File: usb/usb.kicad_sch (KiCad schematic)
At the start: 14 parts, among them J101 DX07S016JA3, J102 2x05_Horizontal

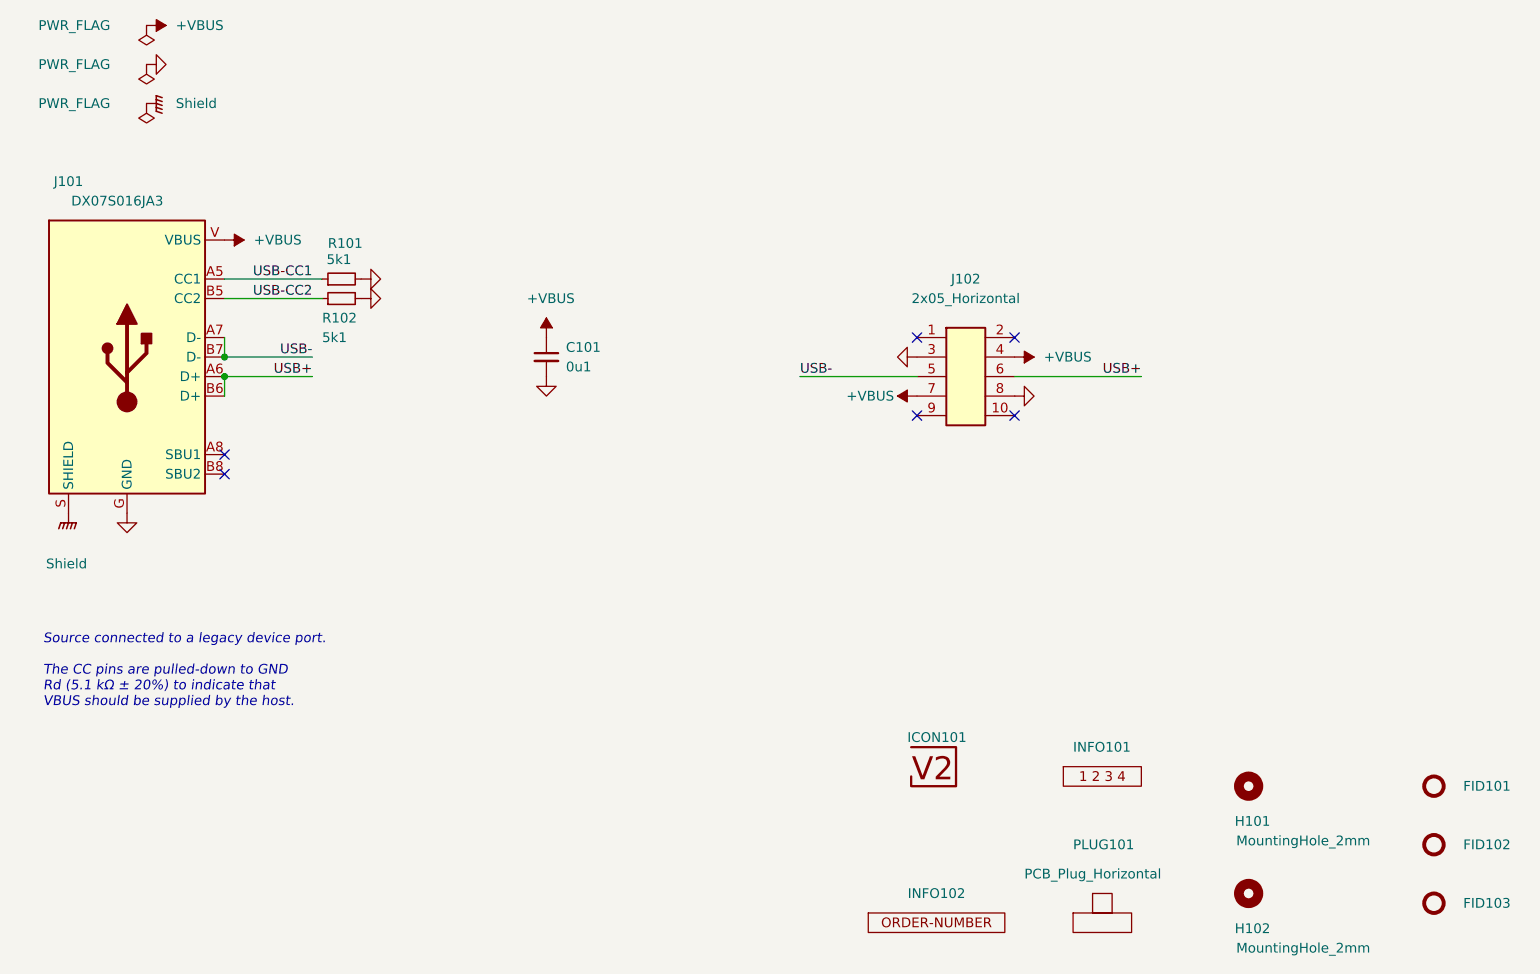
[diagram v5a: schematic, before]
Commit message: Replace Order_Number
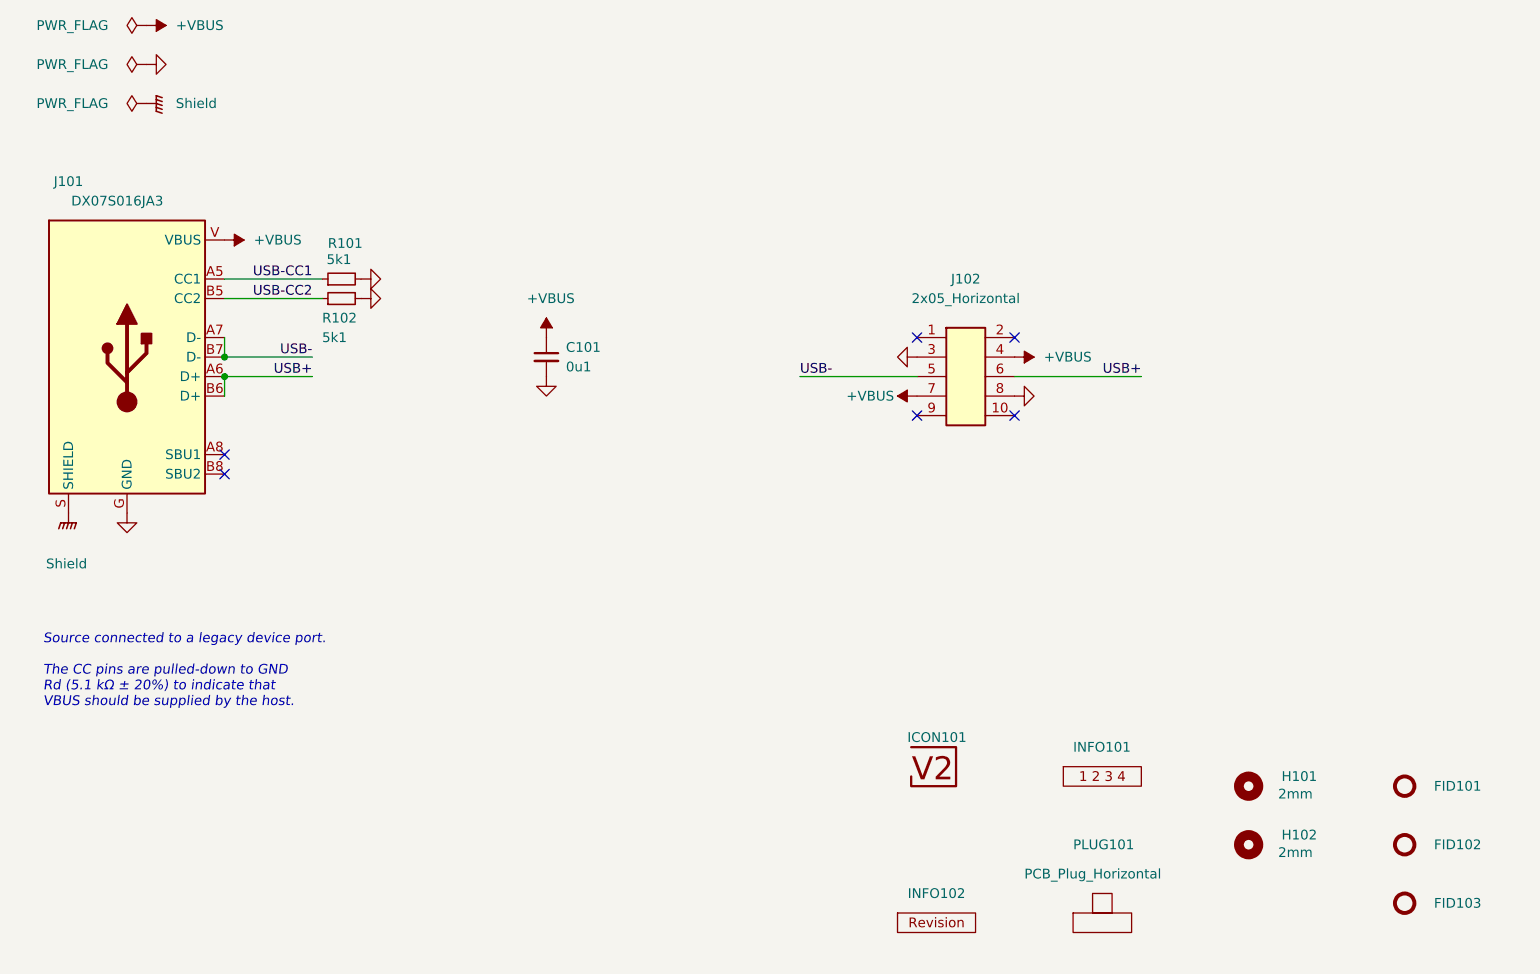
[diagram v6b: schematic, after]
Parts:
- H101, H102: value MountingHole_2mm -> 2mm
- INFO102: value Order_Number -> ~; footprint V2_Production:Order_Number -> V2_Production:Revision; symbol V2_Production:Order_Number -> V2_Production:Revision
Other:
- moved on the sheet: FID101, FID102, FID103, H102
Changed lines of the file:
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@@
 		(dnp no)
 		(property "Reference" "H101"
-			(at 246.888 162.052 0)
-			(effects
-				(font
-					(size 1.27 1.27)
-				)
-			)
-		)
-		(property "Value" "MountingHole_2mm"
-			(at 253.492 164.592 0)
+			(at 252.984 156.21 0)
+			(effects
+				(font
+					(size 1.27 1.27)
+				)
+			)
+		)
+		(property "Value" "2mm"
+			(at 252.476 158.496 0)
 			(effects
 				(font
@@
 			)
 		)
-		(property "Sim.Enable" "0"
-			(at 246.38 157.48 0)
-			(effects
-				(font
-					(size 1.27 1.27)
-				)
-				(hide yes)
-			)
-		)
 		(instances
 			(project "usb"
@@
 	(symbol
 		(lib_id "V2_power:PWR_FLAG")
-		(at 102.87 68.58 90)
+		(at 102.87 68.58 0)
 		(unit 1)
 		(exclude_from_sim no)
@@
 		(dnp no)
 		(property "Reference" "#FLG0103"
-			(at 100.965 68.58 0)
+			(at 102.87 66.675 0)
 			(effects
 				(font
@@
 		)
 		(property "Value" "PWR_FLAG"
-			(at 93.472 68.58 90)
+			(at 93.218 68.58 0)
 			(effects
 				(font
@@
 		)
 		(property "Description" "Special symbol for telling ERC where power comes from"
-			(at 120.142 68.58 0)
+			(at 102.87 85.852 0)
 			(effects
 				(font
@@
 	(symbol
 		(lib_id "V2_Mechanical:MountingHole_2mm")
-		(at 246.38 171.45 0)
+		(at 246.38 165.1 0)
 		(unit 1)
 		(exclude_from_sim no)
@@
 		(dnp no)
 		(property "Reference" "H102"
-			(at 246.888 176.022 0)
-			(effects
-				(font
-					(size 1.27 1.27)
-				)
-			)
-		)
-		(property "Value" "MountingHole_2mm"
-			(at 253.492 178.562 0)
+			(at 252.984 163.83 0)
+			(effects
+				(font
+					(size 1.27 1.27)
+				)
+			)
+		)
+		(property "Value" "2mm"
+			(at 252.476 166.116 0)
 			(effects
 				(font
@@
 		)
 		(property "Footprint" "V2_Mechanical:MountingHole_2mm"
-			(at 246.38 176.53 0)
-			(effects
-				(font
-					(size 1.27 1.27)
-				)
-				(hide yes)
-			)
-		)
-		(property "Datasheet" ""
-			(at 246.38 171.45 0)
+			(at 246.38 170.18 0)
+			(effects
+				(font
+					(size 1.27 1.27)
+				)
+				(hide yes)
+			)
+		)
+		(property "Datasheet" ""
+			(at 246.38 165.1 0)
 			(effects
 				(font
@@
 		)
 		(property "Description" "Mounting Hole without connection"
-			(at 246.38 171.45 0)
-			(effects
-				(font
-					(size 1.27 1.27)
-				)
-				(hide yes)
-			)
-		)
-		(property "Sim.Enable" "0"
-			(at 246.38 171.45 0)
+			(at 246.38 165.1 0)
 			(effects
 				(font
@@
 	(symbol
 		(lib_id "V2_power:PWR_FLAG")
-		(at 102.87 63.5 90)
+		(at 102.87 63.5 0)
 		(unit 1)
 		(exclude_from_sim no)
@@
 		(dnp no)
 		(property "Reference" "#FLG0102"
-			(at 100.965 63.5 0)
+			(at 102.87 61.595 0)
 			(effects
 				(font
@@
 		)
 		(property "Value" "PWR_FLAG"
-			(at 93.472 63.5 90)
+			(at 93.218 63.5 0)
 			(effects
 				(font
@@
 		)
 		(property "Description" "Special symbol for telling ERC where power comes from"
-			(at 120.142 63.5 0)
+			(at 102.87 80.772 0)
 			(effects
 				(font
@@
 		(at 227.33 173.99 0)
 		(unit 1)
-		(exclude_from_sim no)
+		(exclude_from_sim yes)
 		(in_bom no)
 		(on_board yes)
@@
 			)
 		)
-		(property "Sim.Enable" "0"
-			(at 227.33 173.99 0)
-			(effects
-				(font
-					(size 1.27 1.27)
-				)
-				(hide yes)
-			)
-		)
 		(instances
 			(project "usb"
@@
 	)
 	(symbol
-		(lib_id "V2_Production:Order_Number")
+		(lib_id "V2_Production:Revision")
 		(at 205.74 175.26 0)
 		(unit 1)
@@
 			)
 		)
-		(property "Value" "Order_Number"
+		(property "Value" "~"
 			(at 205.74 177.8 0)
 			(effects
@@
 			)
 		)
-		(property "Footprint" "V2_Production:Order_Number"
+		(property "Footprint" "V2_Production:Revision"
 			(at 205.74 180.34 0)
 			(effects
@@
 	(symbol
 		(lib_id "V2_Mechanical:Fiducial_Paste")
-		(at 270.51 157.48 0)
+		(at 266.7 157.48 0)
 		(unit 1)
 		(exclude_from_sim no)
@@
 		(dnp no)
 		(property "Reference" "FID101"
-			(at 274.32 157.48 0)
+			(at 270.51 157.48 0)
 			(effects
 				(font
@@
 		)
 		(property "Value" "Fiducial_Paste"
-			(at 267.97 153.67 0)
+			(at 264.16 153.67 0)
 			(effects
 				(font
@@
 		)
 		(property "Footprint" "V2_Fiducial:Fiducial_0.5mm_Mask1mm_Paste"
-			(at 270.51 162.56 0)
-			(effects
-				(font
-					(size 1.27 1.27)
-				)
-				(hide yes)
-			)
-		)
-		(property "Datasheet" ""
-			(at 270.51 157.48 0)
+			(at 266.7 162.56 0)
+			(effects
+				(font
+					(size 1.27 1.27)
+				)
+				(hide yes)
+			)
+		)
+		(property "Datasheet" ""
+			(at 266.7 157.48 0)
 			(effects
 				(font
@@
 		)
 		(property "Description" "Fiducial Marker"
-			(at 270.51 157.48 0)
+			(at 266.7 157.48 0)
 			(effects
 				(font
@@
 	(symbol
 		(lib_id "V2_Mechanical:Fiducial_Paste")
-		(at 270.51 165.1 0)
+		(at 266.7 165.1 0)
 		(unit 1)
 		(exclude_from_sim no)
@@
 		(dnp no)
 		(property "Reference" "FID102"
-			(at 274.32 165.1 0)
+			(at 270.51 165.1 0)
 			(effects
 				(font
@@
 		)
 		(property "Value" "Fiducial_Paste"
-			(at 271.78 161.29 0)
+			(at 267.97 161.29 0)
 			(effects
 				(font
@@
 		)
 		(property "Footprint" "V2_Fiducial:Fiducial_0.5mm_Mask1mm_Paste"
-			(at 270.51 170.18 0)
-			(effects
-				(font
-					(size 1.27 1.27)
-				)
-				(hide yes)
-			)
-		)
-		(property "Datasheet" ""
-			(at 270.51 165.1 0)
+			(at 266.7 170.18 0)
+			(effects
+				(font
+					(size 1.27 1.27)
+				)
+				(hide yes)
+			)
+		)
+		(property "Datasheet" ""
+			(at 266.7 165.1 0)
 			(effects
 				(font
@@
 		)
 		(property "Description" "Fiducial Marker"
-			(at 270.51 165.1 0)
+			(at 266.7 165.1 0)
 			(effects
 				(font
@@
 	(symbol
 		(lib_id "V2_power:PWR_FLAG")
-		(at 102.87 58.42 90)
+		(at 102.87 58.42 0)
 		(unit 1)
 		(exclude_from_sim no)
@@
 		(dnp no)
 		(property "Reference" "#FLG0101"
-			(at 100.965 58.42 0)
+			(at 102.87 56.515 0)
 			(effects
 				(font
@@
 		)
 		(property "Value" "PWR_FLAG"
-			(at 93.472 58.42 90)
+			(at 93.218 58.42 0)
 			(effects
 				(font
@@
 		)
 		(property "Description" "Special symbol for telling ERC where power comes from"
-			(at 120.142 58.42 0)
+			(at 102.87 75.692 0)
 			(effects
 				(font
@@
 	(symbol
 		(lib_id "V2_Mechanical:Fiducial_Paste")
-		(at 270.51 172.72 0)
+		(at 266.7 172.72 0)
 		(unit 1)
 		(exclude_from_sim no)
@@
 		(dnp no)
 		(property "Reference" "FID103"
-			(at 274.32 172.72 0)
+			(at 270.51 172.72 0)
 			(effects
 				(font
@@
 		)
 		(property "Value" "Fiducial_Paste"
-			(at 267.97 168.91 0)
+			(at 264.16 168.91 0)
 			(effects
 				(font
@@
 		)
 		(property "Footprint" "V2_Fiducial:Fiducial_0.5mm_Mask1mm_Paste"
-			(at 270.51 177.8 0)
-			(effects
-				(font
-					(size 1.27 1.27)
-				)
-				(hide yes)
-			)
-		)
-		(property "Datasheet" ""
-			(at 270.51 172.72 0)
+			(at 266.7 177.8 0)
+			(effects
+				(font
+					(size 1.27 1.27)
+				)
+				(hide yes)
+			)
+		)
+		(property "Datasheet" ""
+			(at 266.7 172.72 0)
 			(effects
 				(font
@@
 		)
 		(property "Description" "Fiducial Marker"
-			(at 270.51 172.72 0)
+			(at 266.7 172.72 0)
 			(effects
 				(font
@@
 			(at 205.74 154.94 0)
 			(effects
-				(font
-					(size 1.27 1.27)
-				)
-				(hide yes)
-			)
-		)
-		(property "Sim.Enable" "0"
-			(at 205.74 154.94 0)
-			(effects

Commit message: Update Library
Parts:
- C101: symbol V2_Device:C_0603_0u1 -> V2_Capacitor:0603_0u1
- R101, R102: symbol V2_Device:R_0603_5k1 -> V2_Resistor:0603_5k1
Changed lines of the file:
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@@
 	)
 	(symbol
-		(lib_id "V2_Device:R_0603_5k1")
+		(lib_id "V2_Resistor:0603_5k1")
 		(at 128.27 91.44 90)
 		(unit 1)
@@
 		(dnp no)
 		(fields_autoplaced yes)
-		(property "Reference" "#PWR0106"
+		(property "Reference" "#PWR106"
 			(at 137.16 93.98 0)
 			(effects
@@
 			(project "usb"
 				(path "/6c8448b4-b04d-47e1-934e-e40cbe27a7be"
-					(reference "#PWR0106")
+					(reference "#PWR106")
 					(unit 1)
 				)
@@
 		(dnp no)
 		(fields_autoplaced yes)
-		(property "Reference" "#PWR0105"
+		(property "Reference" "#PWR105"
 			(at 137.16 91.44 0)
 			(effects
@@
 			(project "usb"
 				(path "/6c8448b4-b04d-47e1-934e-e40cbe27a7be"
-					(reference "#PWR0105")
+					(reference "#PWR105")
 					(unit 1)
 				)
@@
 		(on_board yes)
 		(dnp no)
-		(property "Reference" "#PWR0111"
+		(property "Reference" "#PWR111"
 			(at 207.01 106.68 0)
 			(effects
@@
 			(project "usb"
 				(path "/6c8448b4-b04d-47e1-934e-e40cbe27a7be"
-					(reference "#PWR0111")
+					(reference "#PWR111")
 					(unit 1)
 				)
@@
 		(on_board yes)
 		(dnp no)
-		(property "Reference" "#FLG0103"
+		(property "Reference" "#FLG103"
 			(at 102.87 66.675 0)
 			(effects
@@
 			(project "usb"
 				(path "/6c8448b4-b04d-47e1-934e-e40cbe27a7be"
-					(reference "#FLG0103")
+					(reference "#FLG103")
 					(unit 1)
 				)
@@
 		(on_board yes)
 		(dnp no)
-		(property "Reference" "#PWR0107"
+		(property "Reference" "#PWR107"
 			(at 154.94 102.87 0)
 			(effects
@@
 			(project "usb"
 				(path "/6c8448b4-b04d-47e1-934e-e40cbe27a7be"
-					(reference "#PWR0107")
+					(reference "#PWR107")
 					(unit 1)
 				)
@@
 		(on_board yes)
 		(dnp no)
-		(property "Reference" "#PWR0113"
+		(property "Reference" "#PWR113"
 			(at 92.71 128.27 0)
 			(effects
@@
 			(project "usb"
 				(path "/6c8448b4-b04d-47e1-934e-e40cbe27a7be"
-					(reference "#PWR0113")
+					(reference "#PWR113")
 					(unit 1)
 				)
@@
 		(dnp no)
 		(fields_autoplaced yes)
-		(property "Reference" "#PWR0104"
+		(property "Reference" "#PWR104"
 			(at 109.22 86.36 0)
 			(effects
@@
 			(project "usb"
 				(path "/6c8448b4-b04d-47e1-934e-e40cbe27a7be"
-					(reference "#PWR0104")
+					(reference "#PWR104")
 					(unit 1)
 				)
@@
 		(dnp no)
 		(fields_autoplaced yes)
-		(property "Reference" "#PWR0103"
+		(property "Reference" "#PWR103"
 			(at 109.22 68.58 0)
 			(effects
@@
 			(project "usb"
 				(path "/6c8448b4-b04d-47e1-934e-e40cbe27a7be"
-					(reference "#PWR0103")
+					(reference "#PWR103")
 					(unit 1)
 				)
@@
 		(dnp no)
 		(fields_autoplaced yes)
-		(property "Reference" "#PWR0109"
+		(property "Reference" "#PWR109"
 			(at 212.09 101.6 0)
 			(effects
@@
 			(project "usb"
 				(path "/6c8448b4-b04d-47e1-934e-e40cbe27a7be"
-					(reference "#PWR0109")
+					(reference "#PWR109")
 					(unit 1)
 				)
@@
 		(on_board yes)
 		(dnp no)
-		(property "Reference" "#FLG0102"
+		(property "Reference" "#FLG102"
 			(at 102.87 61.595 0)
 			(effects
@@
 			(project "usb"
 				(path "/6c8448b4-b04d-47e1-934e-e40cbe27a7be"
-					(reference "#FLG0102")
+					(reference "#FLG102")
 					(unit 1)
 				)
@@
 		(dnp no)
 		(fields_autoplaced yes)
-		(property "Reference" "#PWR0114"
+		(property "Reference" "#PWR114"
 			(at 100.33 128.27 0)
 			(effects
@@
 			(project "usb"
 				(path "/6c8448b4-b04d-47e1-934e-e40cbe27a7be"
-					(reference "#PWR0114")
+					(reference "#PWR114")
 					(unit 1)
 				)
@@
 		(dnp no)
 		(fields_autoplaced yes)
-		(property "Reference" "#PWR0110"
+		(property "Reference" "#PWR110"
 			(at 154.94 110.49 0)
 			(effects
@@
 			(project "usb"
 				(path "/6c8448b4-b04d-47e1-934e-e40cbe27a7be"
-					(reference "#PWR0110")
+					(reference "#PWR110")
 					(unit 1)
 				)
@@
 		(at 227.33 173.99 0)
 		(unit 1)
-		(exclude_from_sim yes)
+		(exclude_from_sim no)
 		(in_bom no)
 		(on_board yes)
@@
 			)
 		)
+		(property "Sim.Enable" "0"
+			(at 227.33 173.99 0)
+			(effects
+				(font
+					(size 1.27 1.27)
+				)
+				(hide yes)
+			)
+		)
 		(instances
 			(project "usb"
@@
 		(dnp no)
 		(fields_autoplaced yes)
-		(property "Reference" "#PWR0101"
+		(property "Reference" "#PWR101"
 			(at 99.06 58.42 0)
 			(effects
@@
 			(project ""
 				(path "/6c8448b4-b04d-47e1-934e-e40cbe27a7be"
-					(reference "#PWR0101")
+					(reference "#PWR101")
 					(unit 1)
 				)
@@
 		(on_board yes)
 		(dnp no)
-		(property "Reference" "#PWR0112"
+		(property "Reference" "#PWR112"
 			(at 222.25 106.68 0)
 			(effects
@@
 			(project "usb"
 				(path "/6c8448b4-b04d-47e1-934e-e40cbe27a7be"
-					(reference "#PWR0112")
-					(unit 1)
-				)
-			)
-		)
-	)
-	(symbol
-		(lib_id "V2_Device:C_0603_0u1")
+					(reference "#PWR112")
+					(unit 1)
+				)
+			)
+		)
+	)
+	(symbol
+		(lib_id "V2_Capacitor:0603_0u1")
 		(at 154.94 101.6 0)
 		(unit 1)
@@
 		(on_board yes)
 		(dnp no)
-		(property "Reference" "#PWR0108"
+		(property "Reference" "#PWR108"
 			(at 196.85 101.6 0)
 			(effects
@@
 			(project "usb"
 				(path "/6c8448b4-b04d-47e1-934e-e40cbe27a7be"
-					(reference "#PWR0108")
+					(reference "#PWR108")
 					(unit 1)
 				)
@@
 		(dnp no)
 		(fields_autoplaced yes)
-		(property "Reference" "#PWR0102"
+		(property "Reference" "#PWR102"
 			(at 109.22 63.5 0)
 			(effects
@@
 			(project "usb"
 				(path "/6c8448b4-b04d-47e1-934e-e40cbe27a7be"
-					(reference "#PWR0102")
+					(reference "#PWR102")
 					(unit 1)
 				)
@@
 	)
 	(symbol
-		(lib_id "V2_Device:R_0603_5k1")
+		(lib_id "V2_Resistor:0603_5k1")
 		(at 128.27 93.98 90)
 		(unit 1)
@@
 		(on_board yes)
 		(dnp no)
-		(property "Reference" "#FLG0101"
+		(property "Reference" "#FLG101"
 			(at 102.87 56.515 0)
 			(effects
@@
 			(project "usb"
 				(path "/6c8448b4-b04d-47e1-934e-e40cbe27a7be"
-					(reference "#FLG0101")
-					(unit 1)
-				)
+					(reference "#FLG101")
+					(unit 1)
+				)
